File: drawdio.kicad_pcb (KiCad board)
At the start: 2 copper layers, 12 parts, among them P1 CONN_2, P2 SPK, Q1 BC558, Q2 BC547, U1 LM555N

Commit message: Trigged size
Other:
- board outline added: 59.7 x 17.8 mm
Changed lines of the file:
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@@
     (links 23)
     (no_connects 1)
-    (area 72.86281 76.913 132.797572 96.774001)
+    (area 73.584999 78.664999 133.425001 99.135001)
     (thickness 1.6)
-    (drawings 0)
+    (drawings 8)
     (tracks 54)
     (zones 0)
@@
     )
   )
+  (gr_line (start 73.66 93.98) (end 73.66 83.82) (angle 90) (layer Edge.Cuts) (width 0.15))
+  (gr_line (start 133.35 83.82) (end 133.35 93.98) (angle 90) (layer Edge.Cuts) (width 0.15))
+  (gr_line (start 129.54 97.79) (end 77.47 97.79) (angle 90) (layer Edge.Cuts) (width 0.15))
+  (gr_line (start 77.47 80.01) (end 129.54 80.01) (angle 90) (layer Edge.Cuts) (width 0.15))
+  (gr_arc (start 129.54 93.98) (end 133.35 93.98) (angle 90) (layer Edge.Cuts) (width 0.15))
+  (gr_arc (start 129.54 83.82) (end 129.54 80.01) (angle 90) (layer Edge.Cuts) (width 0.15))
+  (gr_arc (start 77.47 83.82) (end 73.66 83.82) (angle 90) (layer Edge.Cuts) (width 0.15))
+  (gr_arc (start 77.47 93.98) (end 77.47 97.79) (angle 90) (layer Edge.Cuts) (width 0.15))
   (segment (start 118.11 86.4) (end 118.11 86.36) (width 0.508) (layer B.Cu) (net 1))
   (segment (start 105.664 93.472) (end 103.124 90.932) (width 0.508) (layer B.Cu) (net 2))
@@
   (segment (start 110.998 90.678) (end 110.744 90.932) (width 0.508) (layer B.Cu) (net 3))
   (segment (start 114.808 90.678) (end 110.998 90.678) (width 0.508) (layer B.Cu) (net 3))
-  (segment (start 112.014 88.9) (end 118.11 88.9) (width 0.508) (layer B.Cu) (net 4))
-  (segment (start 111.506 88.392) (end 112.014 88.9) (width 0.508) (layer B.Cu) (net 4))
-  (segment (start 110.744 88.392) (end 111.506 88.392) (width 0.508) (layer B.Cu) (net 4))
   (segment (start 119.634 88.9) (end 124.206 84.328) (width 0.508) (layer B.Cu) (net 4))
   (segment (start 118.11 88.9) (end 119.634 88.9) (width 0.508) (layer B.Cu) (net 4))
+  (segment (start 112.014 88.646) (end 118.11 88.646) (width 0.508) (layer B.Cu) (net 4))
+  (segment (start 111.506 88.392) (end 112.014 88.646) (width 0.508) (layer B.Cu) (net 4))
+  (segment (start 110.744 88.392) (end 111.506 88.392) (width 0.508) (layer B.Cu) (net 4))
   (segment (start 108.204 88.392) (end 105.664 85.852) (width 0.508) (layer B.Cu) (net 4))
   (segment (start 105.664 85.852) (end 103.124 85.852) (width 0.508) (layer B.Cu) (net 4))

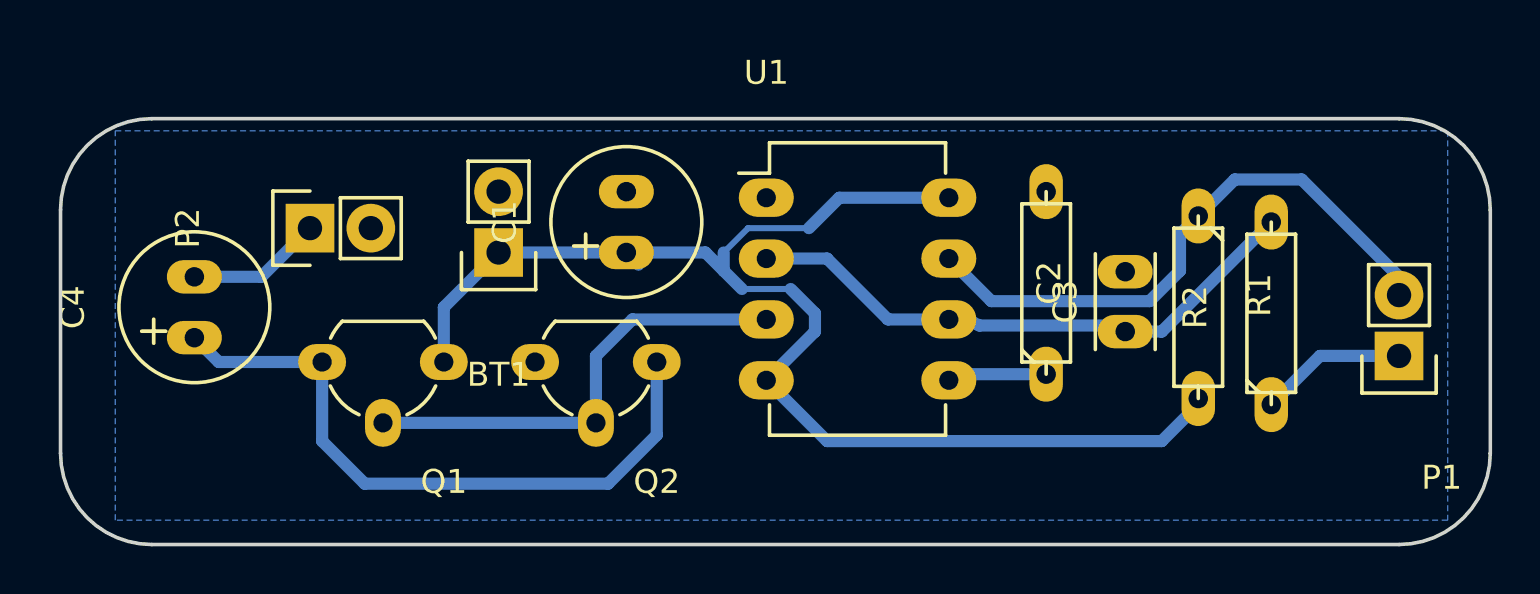
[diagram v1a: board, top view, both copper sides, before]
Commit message: smaller board
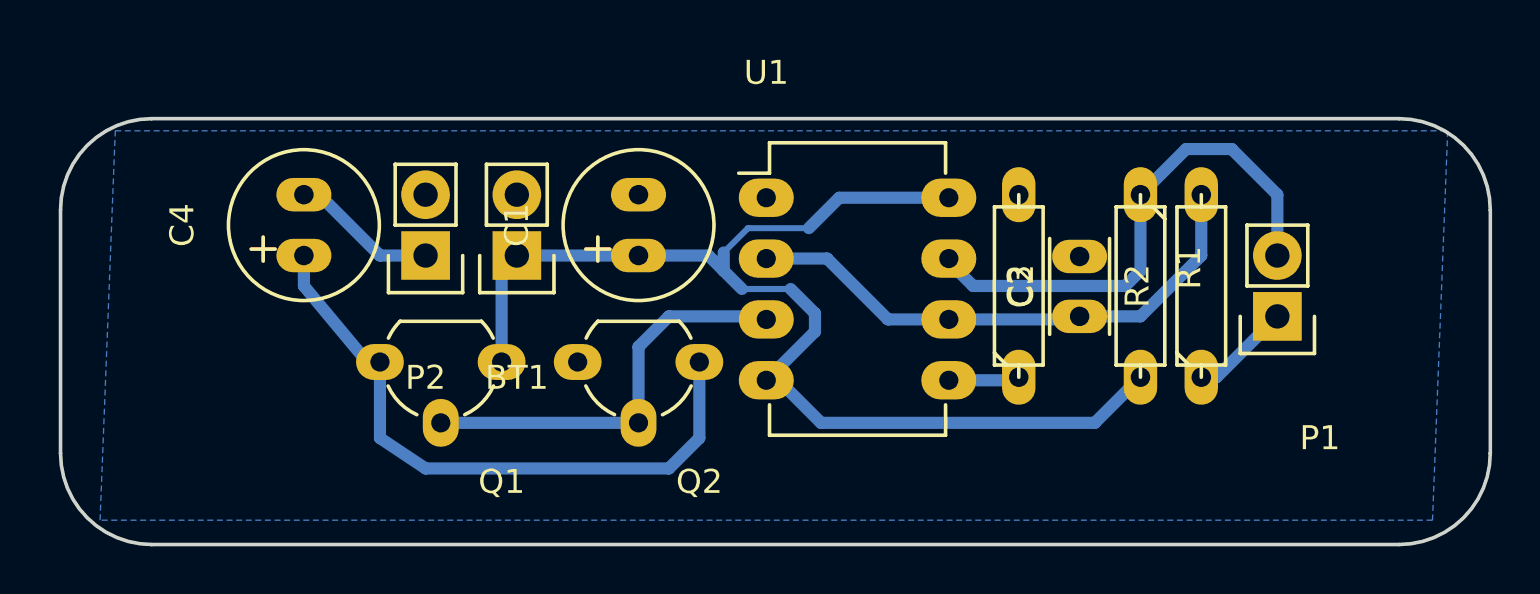
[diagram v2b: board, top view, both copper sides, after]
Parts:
- moved C4 5.71 mm to (83.8, 85.7)
- moved P1 5.34 mm to (124.5, 88.3)
- moved P2 4.96 mm to (88.9, 85.7), turned to 180 degrees
- moved R1 3.14 mm to (121.3, 87.0)
- moved R2 2.57 mm to (118.7, 87.0)
- moved Q1 2.41 mm to (92.1, 90.2)
- moved C3 2.01 mm to (116.2, 88.3)
- moved Q2 1.78 mm to (100.3, 90.2)
- moved C2 1.15 mm to (113.7, 87.0)
- moved BT1 0.77 mm to (92.7, 85.7)
- moved C1 0.52 mm to (97.8, 85.7)
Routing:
- net VCC: track 55.2 -> 50.3 mm
- net Net-(P1-Pad2): track 25.0 -> 21.8 mm
- net Net-(Q1-Pad2): track 19.4 -> 17.3 mm
- net Net-(P1-Pad1): track 6.18 -> 4.23 mm
- net Net-(C4-Pad1): track 27.7 -> 26.2 mm
- net Net-(C2-Pad1): track 4.17 -> 3.33 mm

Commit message: V0.2
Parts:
- moved C4 3.18 mm to (83.8, 88.9)
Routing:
- net Net-(C4-Pad1): track 26.2 -> 23.7 mm
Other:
- board size 59.7 x 17.8 mm -> 47 x 17 mm
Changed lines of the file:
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@@
     (links 23)
     (no_connects 0)
-    (area 72.86281 76.913 133.425001 97.865001)
+    (area 68.92262 76.913 127.717572 103.825)
     (thickness 1.6)
-    (drawings 8)
+    (drawings 10)
     (tracks 58)
     (zones 0)
@@
     (pad_to_mask_clearance 0)
     (aux_axis_origin 0 0)
-    (visible_elements 7FFFFFFF)
+    (visible_elements 7FFCFFFF)
     (pcbplotparams
       (layerselection 0x00030_80000001)
@@
   )
   (module Capacitors_Elko_ThroughHole:Elko_vert_11.2x6.3mm_RM2.5 (layer F.Cu)
-    (at 83.82 85.725 90)
+    (at 83.82 88.9 90)
     (descr "Electrolytic Capacitor, vertical, diameter 6,3mm, RM 2,5mm, radial,")
     (tags "Electrolytic Capacitor, vertical, diameter 6,3mm, RM 2,5mm, Elko, Electrolytkondensator, Kondensator gepolt, Durchmesser 6,3mm, radial,")
@@
     )
   )
-  (gr_line (start 73.66 93.98) (end 73.66 83.82) (angle 90) (layer Edge.Cuts) (width 0.15))
-  (gr_line (start 133.35 83.82) (end 133.35 93.98) (angle 90) (layer Edge.Cuts) (width 0.15))
-  (gr_line (start 129.54 97.79) (end 77.47 97.79) (angle 90) (layer Edge.Cuts) (width 0.15))
-  (gr_line (start 77.47 80.01) (end 129.54 80.01) (angle 90) (layer Edge.Cuts) (width 0.15))
-  (gr_arc (start 129.54 93.98) (end 133.35 93.98) (angle 90) (layer Edge.Cuts) (width 0.15))
-  (gr_arc (start 129.54 83.82) (end 129.54 80.01) (angle 90) (layer Edge.Cuts) (width 0.15))
-  (gr_arc (start 77.47 83.82) (end 73.66 83.82) (angle 90) (layer Edge.Cuts) (width 0.15))
-  (gr_arc (start 77.47 93.98) (end 77.47 97.79) (angle 90) (layer Edge.Cuts) (width 0.15))
+  (dimension 47 (width 0.25) (layer Eco2.User)
+    (gr_text 47,000mm (at 102.87 101.6) (layer Eco2.User)
+      (effects (font (size 1 1) (thickness 0.25)))
+    )
+    (feature1 (pts (xy 127 96) (xy 127 102.999999)))
+    (feature2 (pts (xy 80 96) (xy 80 102.999999)))
+    (crossbar (pts (xy 80 102.999999) (xy 127 102.999999)))
+    (arrow1a (pts (xy 127 102.999999) (xy 125.873496 103.58642)))
+    (arrow1b (pts (xy 127 102.999999) (xy 125.873496 102.413578)))
+    (arrow2a (pts (xy 80 102.999999) (xy 81.126504 103.58642)))
+    (arrow2b (pts (xy 80 102.999999) (xy 81.126504 102.413578)))
+  )
+  (dimension 17 (width 0.25) (layer Eco2.User)
+    (gr_text 17,000mm (at 71.12 87.63 90) (layer Eco2.User)
+      (effects (font (size 1 1) (thickness 0.25)))
+    )
+    (feature1 (pts (xy 80 79) (xy 73 79)))
+    (feature2 (pts (xy 80 96) (xy 73 96)))
+    (crossbar (pts (xy 73 96) (xy 73 79)))
+    (arrow1a (pts (xy 73 79) (xy 73.586421 80.126504)))
+    (arrow1b (pts (xy 73 79) (xy 72.413579 80.126504)))
+    (arrow2a (pts (xy 73 96) (xy 73.586421 94.873496)))
+    (arrow2b (pts (xy 73 96) (xy 72.413579 94.873496)))
+  )
+  (gr_line (start 80 80) (end 80 95) (angle 90) (layer Edge.Cuts) (width 0.15))
+  (gr_line (start 126 79) (end 81 79) (angle 90) (layer Edge.Cuts) (width 0.15))
+  (gr_line (start 127 95) (end 127 80) (angle 90) (layer Edge.Cuts) (width 0.15))
+  (gr_line (start 81 96) (end 126 96) (angle 90) (layer Edge.Cuts) (width 0.15))
+  (gr_arc (start 81 95) (end 81 96) (angle 90) (layer Edge.Cuts) (width 0.15))
+  (gr_arc (start 81 80) (end 80 80) (angle 90) (layer Edge.Cuts) (width 0.15))
+  (gr_arc (start 126 80) (end 126 79) (angle 90) (layer Edge.Cuts) (width 0.15))
+  (gr_arc (start 126 95) (end 127 95) (angle 90) (layer Edge.Cuts) (width 0.15))
   (segment (start 100.711 85.725) (end 101.346 86.36) (width 0.508) (layer B.Cu) (net 2))
-  (segment (start 97.79 85.725) (end 100.711 85.725) (width 0.508) (layer B.Cu) (net 2) (status 400000))
-  (segment (start 92.71 85.725) (end 97.79 85.725) (width 0.508) (layer B.Cu) (net 2) (status C00000))
-  (segment (start 92.71 85.725) (end 92.075 86.36) (width 0.508) (layer B.Cu) (net 2) (status C00000))
-  (segment (start 92.075 86.36) (end 92.075 90.17) (width 0.508) (layer B.Cu) (net 2) (status C00000))
+  (segment (start 97.79 85.725) (end 100.711 85.725) (width 0.508) (layer B.Cu) (net 2))
+  (segment (start 92.71 85.725) (end 97.79 85.725) (width 0.508) (layer B.Cu) (net 2))
+  (segment (start 92.71 85.725) (end 92.075 86.36) (width 0.508) (layer B.Cu) (net 2))
+  (segment (start 92.075 86.36) (end 92.075 90.17) (width 0.508) (layer B.Cu) (net 2))
   (segment (start 103.124 90.932) (end 103.632 90.932) (width 0.508) (layer B.Cu) (net 2))
   (segment (start 103.632 90.932) (end 105.41 92.71) (width 0.508) (layer B.Cu) (net 2))
@@
   (segment (start 108.204 88.392) (end 105.664 85.852) (width 0.508) (layer B.Cu) (net 4))
   (segment (start 110.744 88.392) (end 111.506 88.392) (width 0.508) (layer B.Cu) (net 4))
-  (segment (start 83.82 83.185) (end 84.455 83.185) (width 0.508) (layer B.Cu) (net 5) (status C00000))
-  (segment (start 84.455 83.185) (end 86.995 85.725) (width 0.508) (layer B.Cu) (net 5) (status 400000))
-  (segment (start 86.995 85.725) (end 88.9 85.725) (width 0.508) (layer B.Cu) (net 5) (status 800000))
-  (segment (start 100.33 90.17) (end 100.33 93.345) (width 0.508) (layer B.Cu) (net 6) (status 400000))
+  (segment (start 83.82 86.36) (end 88.265 86.36) (width 0.508) (layer B.Cu) (net 5) (status C00000))
+  (segment (start 88.265 86.36) (end 88.9 85.725) (width 0.508) (layer B.Cu) (net 5) (status C00000))
+  (segment (start 88.265 86.36) (end 88.9 85.725) (width 0.508) (layer B.Cu) (net 5))
+  (segment (start 100.33 90.17) (end 100.33 93.345) (width 0.508) (layer B.Cu) (net 6))
   (segment (start 86.995 93.345) (end 86.995 90.805) (width 0.508) (layer B.Cu) (net 6))
   (segment (start 88.9 94.615) (end 86.995 93.345) (width 0.508) (layer B.Cu) (net 6))
   (segment (start 99.06 94.615) (end 88.9 94.615) (width 0.508) (layer B.Cu) (net 6))
   (segment (start 100.33 93.345) (end 99.06 94.615) (width 0.508) (layer B.Cu) (net 6))
-  (segment (start 86.995 90.805) (end 83.82 86.995) (width 0.508) (layer B.Cu) (net 6))
-  (segment (start 83.82 86.995) (end 83.82 85.725) (width 0.508) (layer B.Cu) (net 6) (status 800000))
+  (segment (start 85.09 90.17) (end 83.82 88.9) (width 0.508) (layer B.Cu) (net 6))
+  (segment (start 86.995 90.17) (end 85.09 90.17) (width 0.508) (layer B.Cu) (net 6))
   (segment (start 121.285 90.805) (end 121.92 90.805) (width 0.508) (layer B.Cu) (net 7))
   (segment (start 121.92 90.805) (end 124.46 88.265) (width 0.508) (layer B.Cu) (net 7))
@@
   (segment (start 118.745 86.36) (end 118.11 86.995) (width 0.508) (layer B.Cu) (net 8))
   (segment (start 110.744 85.979) (end 110.744 85.852) (width 0.508) (layer B.Cu) (net 8))
-  (segment (start 89.535 92.71) (end 97.79 92.71) (width 0.508) (layer B.Cu) (net 9) (status C00000))
-  (segment (start 97.79 92.71) (end 97.79 89.535) (width 0.508) (layer B.Cu) (net 9) (status 400000))
+  (segment (start 89.535 92.71) (end 97.79 92.71) (width 0.508) (layer B.Cu) (net 9))
+  (segment (start 97.79 92.71) (end 97.79 89.535) (width 0.508) (layer B.Cu) (net 9))
   (segment (start 97.79 89.535) (end 99.06 88.265) (width 0.508) (layer B.Cu) (net 9))
-  (segment (start 99.06 88.265) (end 102.997 88.265) (width 0.508) (layer B.Cu) (net 9) (status 800000))
-  (segment (start 102.997 88.265) (end 103.124 88.392) (width 0.508) (layer B.Cu) (net 9) (status C00000))
+  (segment (start 99.06 88.265) (end 102.997 88.265) (width 0.508) (layer B.Cu) (net 9))
+  (segment (start 102.997 88.265) (end 103.124 88.392) (width 0.508) (layer B.Cu) (net 9))
   (zone (net 1) (net_name GND) (layer B.Cu) (hatch edge 0.508)
     (connect_pads (clearance 0.508))
@@
     (polygon
       (pts
-        (xy 130.937 96.774) (xy 75.311 96.774) (xy 75.946 80.518) (xy 131.572 80.518)
+        (xy 119.38 88.9) (xy 99.06 88.9) (xy 99.06 93.98) (xy 86.36 93.98) (xy 86.36 80.01)
+        (xy 119.38 80.01)
       )
     )

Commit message: V0.2
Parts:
- P2: value SPK -> CONN_01X01; footprint Pin_Headers:Pin_Header_Straight_1x02 -> Pin_Headers:Pin_Header_Straight_1x01
- Q1, Q2: footprint Housings_TO-92:TO-92_Molded_Wide_Oval -> drawdio:TO-92_JorFru_compact
- moved Q1 3.86 mm to (89.4, 87.4), turned to 270 degrees
- moved Q2 3.82 mm to (96.5, 90.4), turned to 0 degrees
- moved P2 2.41 mm to (88.9, 83.3)
- moved R1 0.18 mm to (121.4, 86.9)
- moved C2 0.18 mm to (113.8, 86.9)
- moved R2 0.18 mm to (118.9, 86.9)
- moved C3 0.18 mm to (116.3, 88.4)
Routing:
- net Net-(C4-Pad1): track 23.7 -> 13.0 mm
- net Net-(Q1-Pad2): track 17.3 -> 13.3 mm
- net VCC: track 50.3 -> 51.7 mm
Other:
- board size 47 x 17 mm -> 45.7 x 12.7 mm

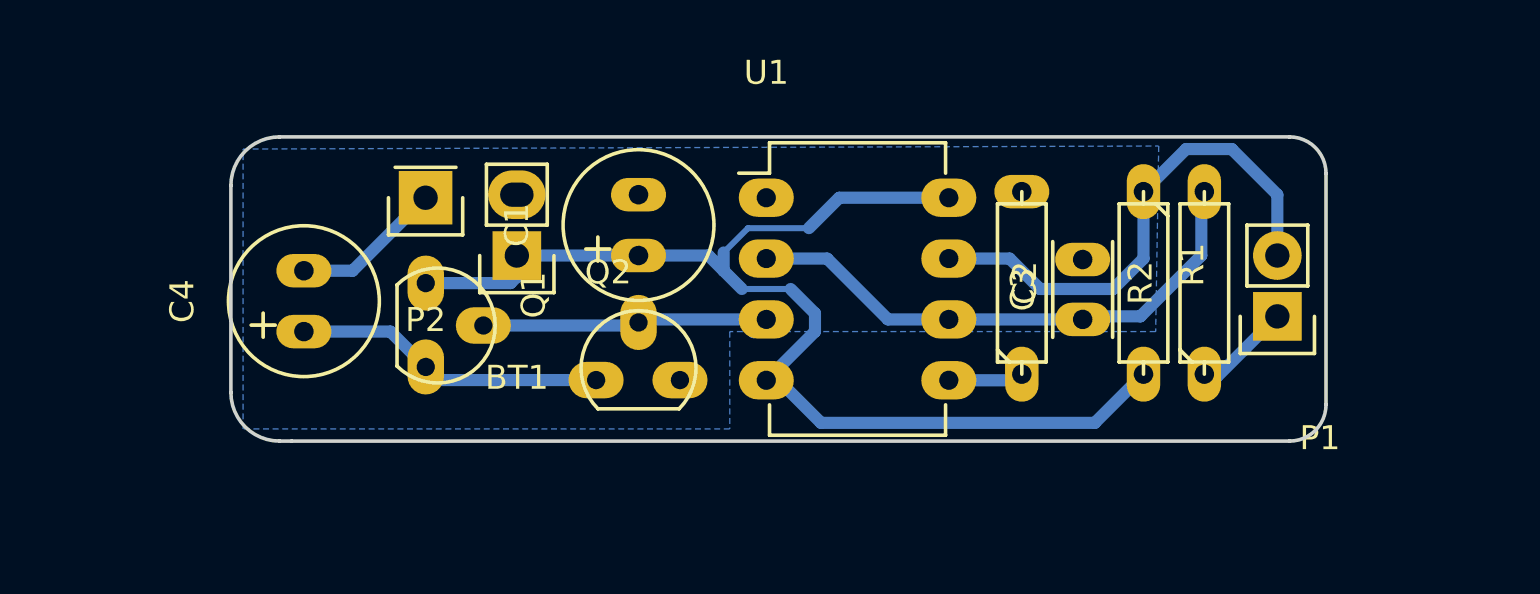
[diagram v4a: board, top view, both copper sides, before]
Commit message: Add GND plane in front layer
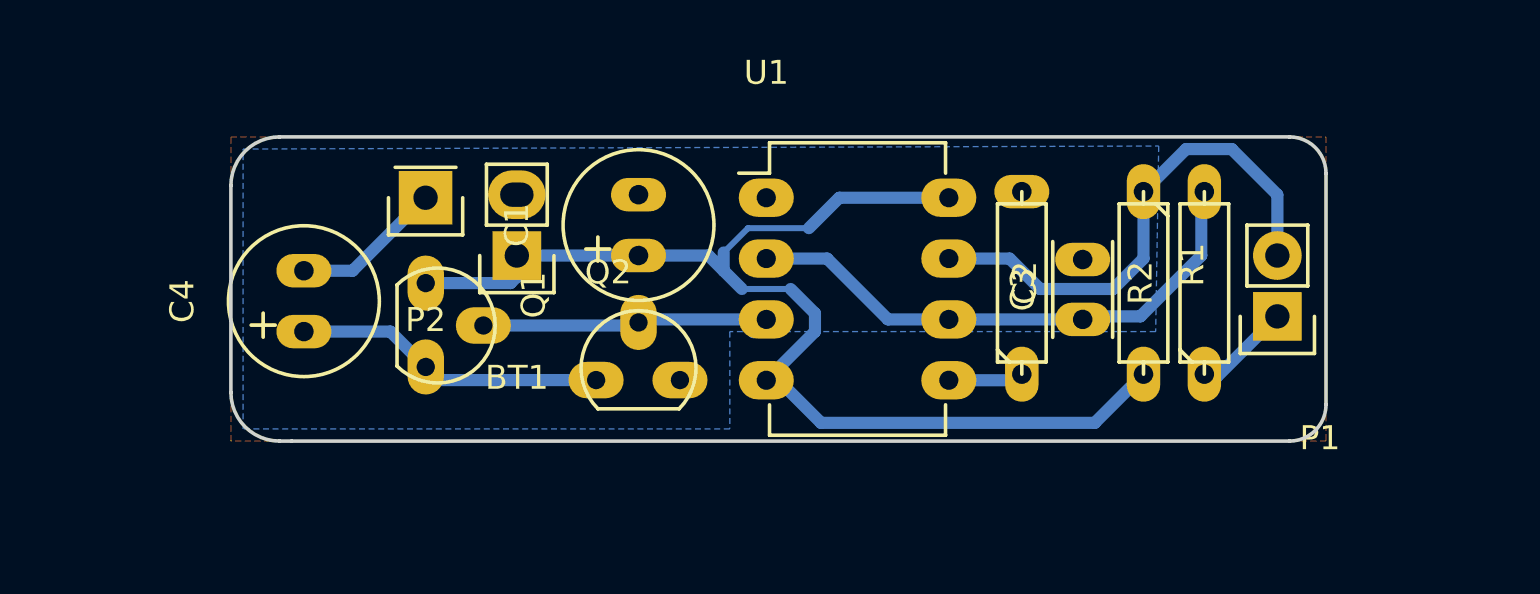
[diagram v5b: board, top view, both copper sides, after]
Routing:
- added copper zone on F.Cu, net GND
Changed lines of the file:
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@@
-(kicad_pcb (version 4) (host pcbnew "(after 2015-mar-04 BZR unknown)-product")
+(kicad_pcb (version 4) (host pcbnew 0.201509081510+6169~29~ubuntu14.04.1-product)
   (general
     (links 22)
     (no_connects 0)
-    (area 80.696999 80.696999 126.567001 93.547001)
+    (area 71.10662 76.913 127.717572 97.536)
     (thickness 1.6)
     (drawings 11)
@@
       )
     )
+  )
+  (zone (net 1) (net_name GND) (layer F.Cu) (hatch edge 0.508)
+    (connect_pads (clearance 0.508))
+    (min_thickness 0.254)
+    (fill yes (arc_segments 16) (thermal_gap 0.508) (thermal_bridge_width 0.508))
+    (polygon
+      (pts
+        (xy 126.492 93.472) (xy 80.772 93.472) (xy 80.772 80.772) (xy 126.492 80.772) (xy 126.492 93.472)
+      )
+    )
